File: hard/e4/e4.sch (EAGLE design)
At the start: 16 parts

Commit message: before net renaming
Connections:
- net +24 renamed +24V
- net PHASE1 renamed PHASE_1
- net PHASE2 renamed PHASE_2
- net PHASE3 renamed PHASE_3
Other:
- note added: "+24V"
- note added: "CAN_H"
- note added: "CAN_L"
- note added: "FREQ_RAW"
- note added: "GND"
- note added: "OUT_DRV1"
- note added: "OUT_DRV2"
- note added: "OUT_DRV3"
- note added: "OUT_DRV4"
- note added: "OUT_DRV5"
- note added: "OUT_DRV6"
- note added: "OUT_DRV7"
- note added: "OUT_DRV8"
- note added: "PHASE_1"
- note added: "PHASE_2"
- note added: "PHASE_3"
- note added: "RAW_DISCRETE_1"
- note added: "RS232_RX"
- note added: "RS232_TX"
- note added: "TACHO_RAW"
- note added: "VCC_DRV1"
- note added: "VCC_DRV2"
- note added: "VCC_DRV3"
- note added: "VCC_DRV4"
- note added: "VCC_DRV5"
- note added: "VCC_DRV6"
- note added: "VCC_DRV7"
- note added: "VCC_DRV8"
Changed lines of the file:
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@@
 <setting verticaltext="up"/>
 </settings>
-<grid distance="0.1" unitdist="inch" unit="inch" style="lines" multiple="1" display="yes" altdistance="0.01" altunitdist="inch" altunit="inch"/>
+<grid distance="0.1" unitdist="inch" unit="inch" style="lines" multiple="1" display="no" altdistance="0.01" altunitdist="inch" altunit="inch"/>
 <layers>
 <layer number="1" name="Top" color="4" fill="1" visible="no" active="no"/>
@@
 <text x="187.96" y="157.48" size="1.524" layer="94" rot="MR0">XP5</text>
 <text x="106.68" y="134.62" size="1.524" layer="94">XP12</text>
+<text x="186.69" y="283.845" size="1.524" layer="94" rot="MR0">OUT_DRV1</text>
+<text x="186.69" y="276.225" size="1.524" layer="94" rot="MR0">OUT_DRV1</text>
+<text x="186.69" y="273.685" size="1.524" layer="94" rot="MR0">OUT_DRV2</text>
+<text x="186.69" y="266.065" size="1.524" layer="94" rot="MR0">OUT_DRV2</text>
+<text x="186.69" y="263.525" size="1.524" layer="94" rot="MR0">OUT_DRV3</text>
+<text x="186.69" y="255.905" size="1.524" layer="94" rot="MR0">OUT_DRV3</text>
+<text x="186.69" y="253.365" size="1.524" layer="94" rot="MR0">OUT_DRV4</text>
+<text x="186.69" y="245.745" size="1.524" layer="94" rot="MR0">OUT_DRV4</text>
+<text x="186.69" y="243.205" size="1.524" layer="94" rot="MR0">OUT_DRV5</text>
+<text x="186.69" y="235.585" size="1.524" layer="94" rot="MR0">OUT_DRV5</text>
+<text x="186.69" y="233.045" size="1.524" layer="94" rot="MR0">OUT_DRV6</text>
+<text x="186.69" y="225.425" size="1.524" layer="94" rot="MR0">OUT_DRV6</text>
+<text x="186.69" y="222.885" size="1.524" layer="94" rot="MR0">OUT_DRV7</text>
+<text x="186.69" y="215.265" size="1.524" layer="94" rot="MR0">OUT_DRV7</text>
+<text x="186.69" y="212.725" size="1.524" layer="94" rot="MR0">OUT_DRV8</text>
+<text x="186.69" y="205.105" size="1.524" layer="94" rot="MR0">OUT_DRV8</text>
+<text x="186.69" y="281.305" size="1.524" layer="94" rot="MR0">VCC_DRV1</text>
+<text x="186.69" y="278.765" size="1.524" layer="94" rot="MR0">VCC_DRV1</text>
+<text x="186.69" y="271.145" size="1.524" layer="94" rot="MR0">VCC_DRV2</text>
+<text x="186.69" y="268.605" size="1.524" layer="94" rot="MR0">VCC_DRV2</text>
+<text x="186.69" y="260.985" size="1.524" layer="94" rot="MR0">VCC_DRV3</text>
+<text x="186.69" y="258.445" size="1.524" layer="94" rot="MR0">VCC_DRV3</text>
+<text x="186.69" y="250.825" size="1.524" layer="94" rot="MR0">VCC_DRV4</text>
+<text x="186.69" y="248.285" size="1.524" layer="94" rot="MR0">VCC_DRV4</text>
+<text x="186.69" y="240.665" size="1.524" layer="94" rot="MR0">VCC_DRV5</text>
+<text x="186.69" y="238.125" size="1.524" layer="94" rot="MR0">VCC_DRV5</text>
+<text x="186.69" y="230.505" size="1.524" layer="94" rot="MR0">VCC_DRV6</text>
+<text x="186.69" y="227.965" size="1.524" layer="94" rot="MR0">VCC_DRV6</text>
+<text x="186.69" y="220.345" size="1.524" layer="94" rot="MR0">VCC_DRV7</text>
+<text x="186.69" y="217.805" size="1.524" layer="94" rot="MR0">VCC_DRV7</text>
+<text x="186.69" y="210.185" size="1.524" layer="94" rot="MR0">VCC_DRV8</text>
+<text x="186.69" y="207.645" size="1.524" layer="94" rot="MR0">VCC_DRV8</text>
+<text x="257.81" y="283.845" size="1.524" layer="94">OUT_DRV1</text>
+<text x="257.81" y="281.305" size="1.524" layer="94">VCC_DRV1</text>
+<text x="257.81" y="278.765" size="1.524" layer="94">OUT_DRV2</text>
+<text x="257.81" y="276.225" size="1.524" layer="94">VCC_DRV2</text>
+<text x="257.81" y="273.685" size="1.524" layer="94">OUT_DRV3</text>
+<text x="257.81" y="271.145" size="1.524" layer="94">VCC_DRV3</text>
+<text x="257.81" y="268.605" size="1.524" layer="94">OUT_DRV4</text>
+<text x="257.81" y="266.065" size="1.524" layer="94">VCC_DRV4</text>
+<text x="257.81" y="263.525" size="1.524" layer="94">OUT_DRV5</text>
+<text x="257.81" y="260.985" size="1.524" layer="94">VCC_DRV5</text>
+<text x="257.81" y="258.445" size="1.524" layer="94">OUT_DRV6</text>
+<text x="257.81" y="255.905" size="1.524" layer="94">VCC_DRV6</text>
+<text x="257.81" y="253.365" size="1.524" layer="94">OUT_DRV7</text>
+<text x="257.81" y="250.825" size="1.524" layer="94">VCC_DRV7</text>
+<text x="257.81" y="248.285" size="1.524" layer="94">OUT_DRV8</text>
+<text x="257.81" y="245.745" size="1.524" layer="94">VCC_DRV8</text>
+<text x="186.69" y="154.305" size="1.524" layer="94" rot="MR0">TACHO_RAW</text>
+<text x="186.69" y="151.765" size="1.524" layer="94" rot="MR0">PHASE_1</text>
+<text x="186.69" y="146.685" size="1.524" layer="94" rot="MR0">PHASE_2</text>
+<text x="186.69" y="141.605" size="1.524" layer="94" rot="MR0">PHASE_3</text>
+<text x="186.69" y="149.225" size="1.524" layer="94" rot="MR0">FREQ_RAW</text>
+<text x="260.35" y="154.305" size="1.524" layer="94">TACHO_RAW</text>
+<text x="260.35" y="151.765" size="1.524" layer="94">PHASE_1</text>
+<text x="260.35" y="146.685" size="1.524" layer="94">PHASE_2</text>
+<text x="260.35" y="141.605" size="1.524" layer="94">PHASE_3</text>
+<text x="260.35" y="149.225" size="1.524" layer="94">FREQ_RAW</text>
+<text x="186.69" y="187.325" size="1.524" layer="94" rot="MR0">GND</text>
+<text x="186.69" y="182.245" size="1.524" layer="94" rot="MR0">GND</text>
+<text x="186.69" y="177.165" size="1.524" layer="94" rot="MR0">GND</text>
+<text x="186.69" y="172.085" size="1.524" layer="94" rot="MR0">GND</text>
+<text x="186.69" y="184.785" size="1.524" layer="94" rot="MR0">+24V</text>
+<text x="186.69" y="179.705" size="1.524" layer="94" rot="MR0">+24V</text>
+<text x="186.69" y="174.625" size="1.524" layer="94" rot="MR0">+24V</text>
+<text x="186.69" y="169.545" size="1.524" layer="94" rot="MR0">+24V</text>
+<text x="260.35" y="179.705" size="1.524" layer="94">GND</text>
+<text x="260.35" y="182.245" size="1.524" layer="94">GND</text>
+<text x="260.35" y="184.785" size="1.524" layer="94">+24V</text>
+<text x="260.35" y="187.325" size="1.524" layer="94">+24V</text>
+<text x="107.95" y="128.905" size="1.524" layer="94">CAN_H</text>
+<text x="107.95" y="131.445" size="1.524" layer="94">CAN_L</text>
+<text x="107.95" y="126.365" size="1.524" layer="94">RS232_RX</text>
+<text x="107.95" y="123.825" size="1.524" layer="94">RS232_TX</text>
+<text x="46.99" y="128.905" size="1.524" layer="94" rot="MR0">CAN_H</text>
+<text x="46.99" y="131.445" size="1.524" layer="94" rot="MR0">CAN_L</text>
+<text x="46.99" y="126.365" size="1.524" layer="94" rot="MR0">RS232_RX</text>
+<text x="46.99" y="123.825" size="1.524" layer="94" rot="MR0">RS232_TX</text>
+<text x="107.95" y="342.265" size="1.524" layer="94">RAW_DISCRETE_1</text>
 </plain>
 <instances>
@@
 </segment>
 </net>
-<net name="+24" class="0">
+<net name="+24V" class="0">
 <segment>
 <pinref part="XP3" gate="G$1" pin="1"/>
@@
 </segment>
 </net>
-<net name="PHASE1" class="0">
+<net name="PHASE_1" class="0">
 <segment>
 <wire x1="226.06" y1="152.4" x2="248.92" y2="152.4" width="0.1524" layer="91"/>
@@
 </segment>
 </net>
-<net name="PHASE2" class="0">
+<net name="PHASE_2" class="0">
 <segment>
 <wire x1="226.06" y1="147.32" x2="248.92" y2="147.32" width="0.1524" layer="91"/>
@@
 </segment>
 </net>
-<net name="PHASE3" class="0">
+<net name="PHASE_3" class="0">
 <segment>
 <wire x1="226.06" y1="142.24" x2="248.92" y2="142.24" width="0.1524" layer="91"/>

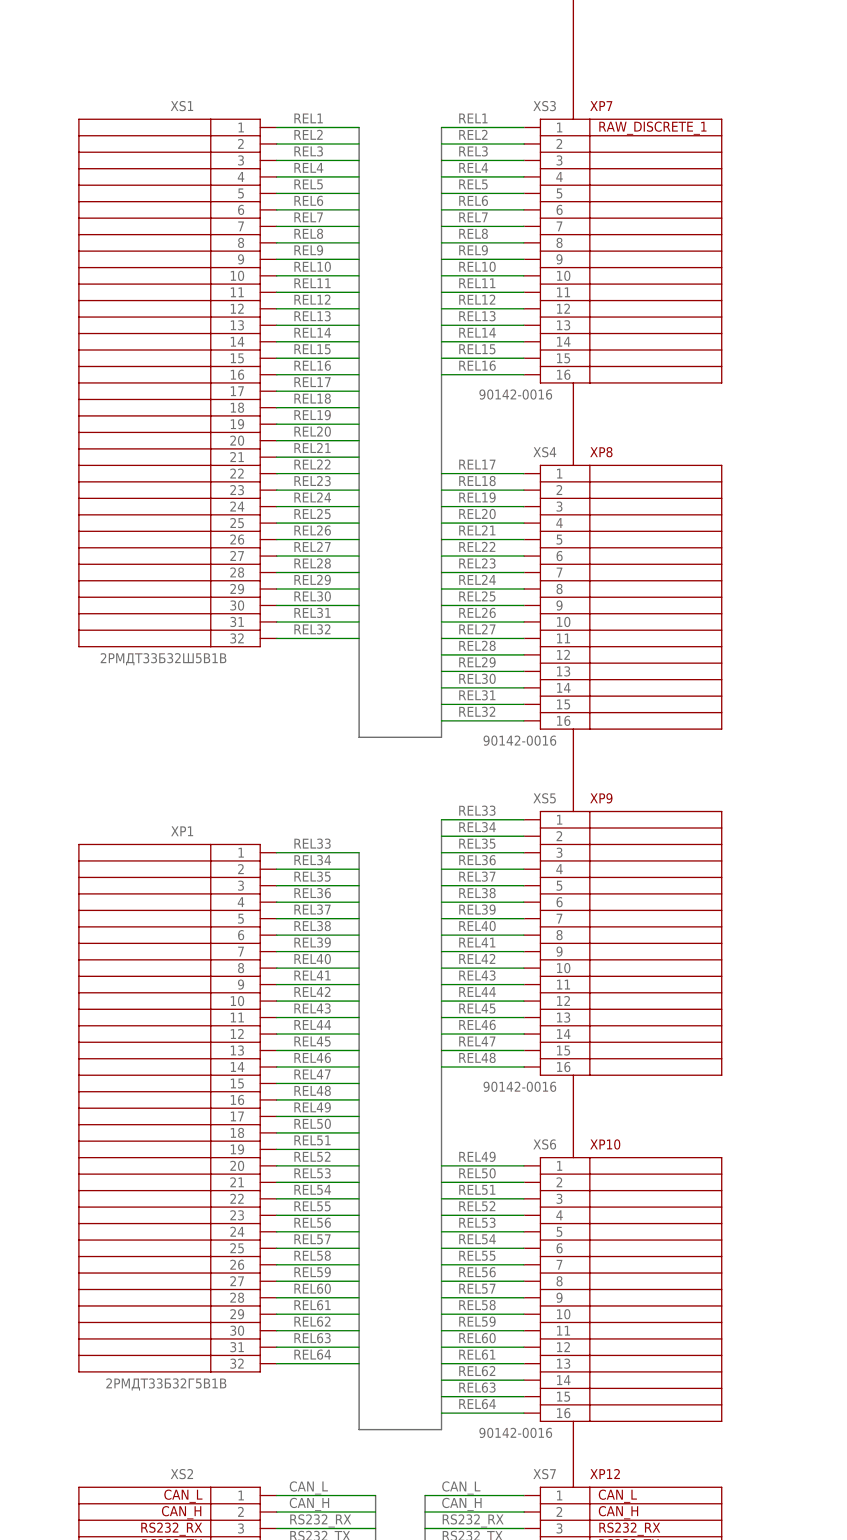
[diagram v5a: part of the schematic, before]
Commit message: nets renamed
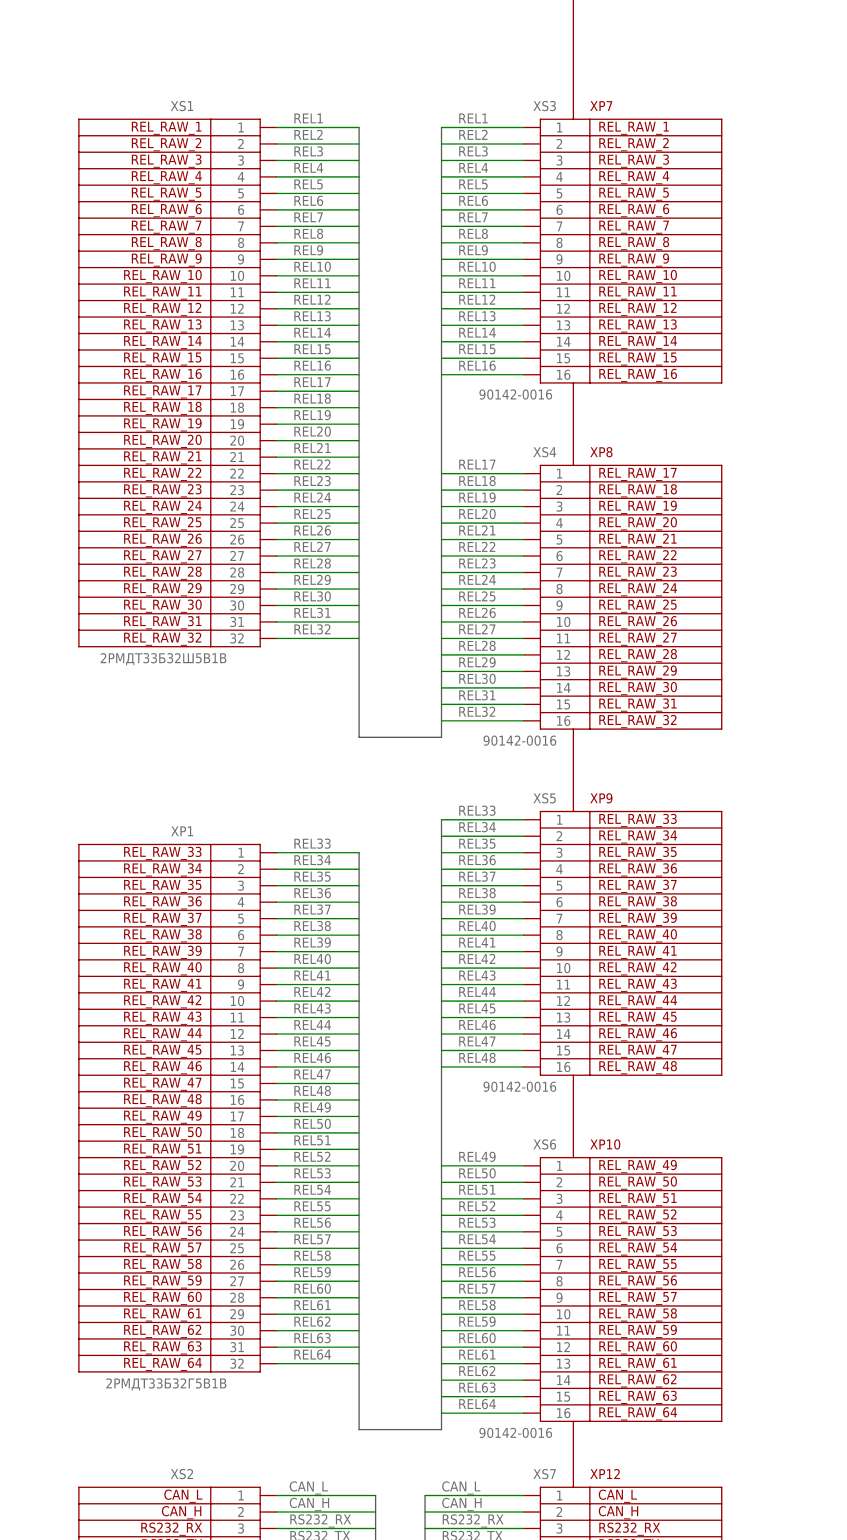
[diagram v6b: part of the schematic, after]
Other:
- note added: "REL_RAW_1"
- note added: "REL_RAW_10"
- note added: "REL_RAW_11"
- note added: "REL_RAW_12"
- note added: "REL_RAW_13"
- note added: "REL_RAW_14"
- note added: "REL_RAW_15"
- note added: "REL_RAW_16"
- note added: "REL_RAW_17"
- note added: "REL_RAW_18"
- note added: "REL_RAW_19"
- note added: "REL_RAW_2"
- note added: "REL_RAW_20"
- note added: "REL_RAW_21"
- note added: "REL_RAW_22"
- note added: "REL_RAW_23"
- note added: "REL_RAW_24"
- note added: "REL_RAW_25"
- note added: "REL_RAW_26"
- note added: "REL_RAW_27"
- note added: "REL_RAW_28"
- note added: "REL_RAW_29"
- note added: "REL_RAW_3"
- note added: "REL_RAW_30"
- note added: "REL_RAW_31"
- note added: "REL_RAW_32"
- note added: "REL_RAW_33"
- note added: "REL_RAW_34"
- note added: "REL_RAW_35"
- note added: "REL_RAW_36"
- note added: "REL_RAW_37"
- note added: "REL_RAW_38"
- note added: "REL_RAW_39"
- note added: "REL_RAW_4"
- note added: "REL_RAW_40"
- note added: "REL_RAW_41"
- note added: "REL_RAW_42"
- note added: "REL_RAW_43"
- note added: "REL_RAW_44"
- note added: "REL_RAW_45"
- note added: "REL_RAW_46"
- note added: "REL_RAW_47"
- note added: "REL_RAW_48"
- note added: "REL_RAW_49"
- note added: "REL_RAW_5"
- note added: "REL_RAW_50"
- note added: "REL_RAW_51"
- note added: "REL_RAW_52"
- note added: "REL_RAW_53"
- note added: "REL_RAW_54"
- note added: "REL_RAW_55"
- note added: "REL_RAW_56"
- note added: "REL_RAW_57"
- note added: "REL_RAW_58"
- note added: "REL_RAW_59"
- note added: "REL_RAW_6"
- note added: "REL_RAW_60"
- note added: "REL_RAW_61"
- note added: "REL_RAW_62"
- note added: "REL_RAW_63"
- note added: "REL_RAW_64"
- note added: "REL_RAW_7"
- note added: "REL_RAW_8"
- note added: "REL_RAW_9"
- note removed: "RAW_DISCRETE_1"
